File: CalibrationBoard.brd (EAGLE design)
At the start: 100 x 80 mm, 56 parts, among them Q1 N-HEXFET-2D_SOT232-, U1 MAX6225ACSA+, U2 MAX6250ACSA+, U3 MAX6126AASA50+

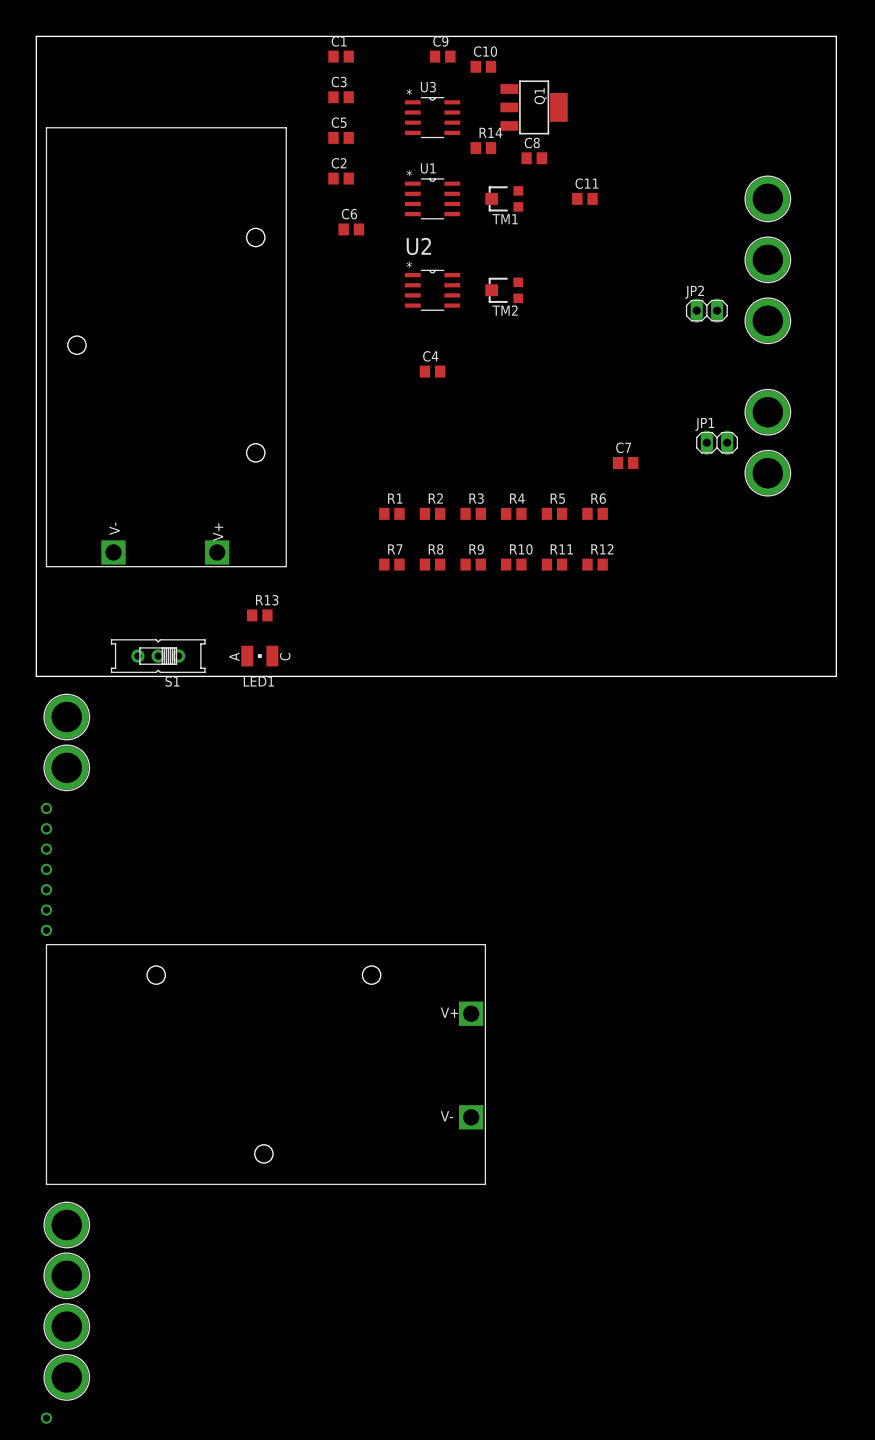
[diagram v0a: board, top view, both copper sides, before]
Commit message: Updates to CAD layout
moved TH to top side, SMDs are on bottom side
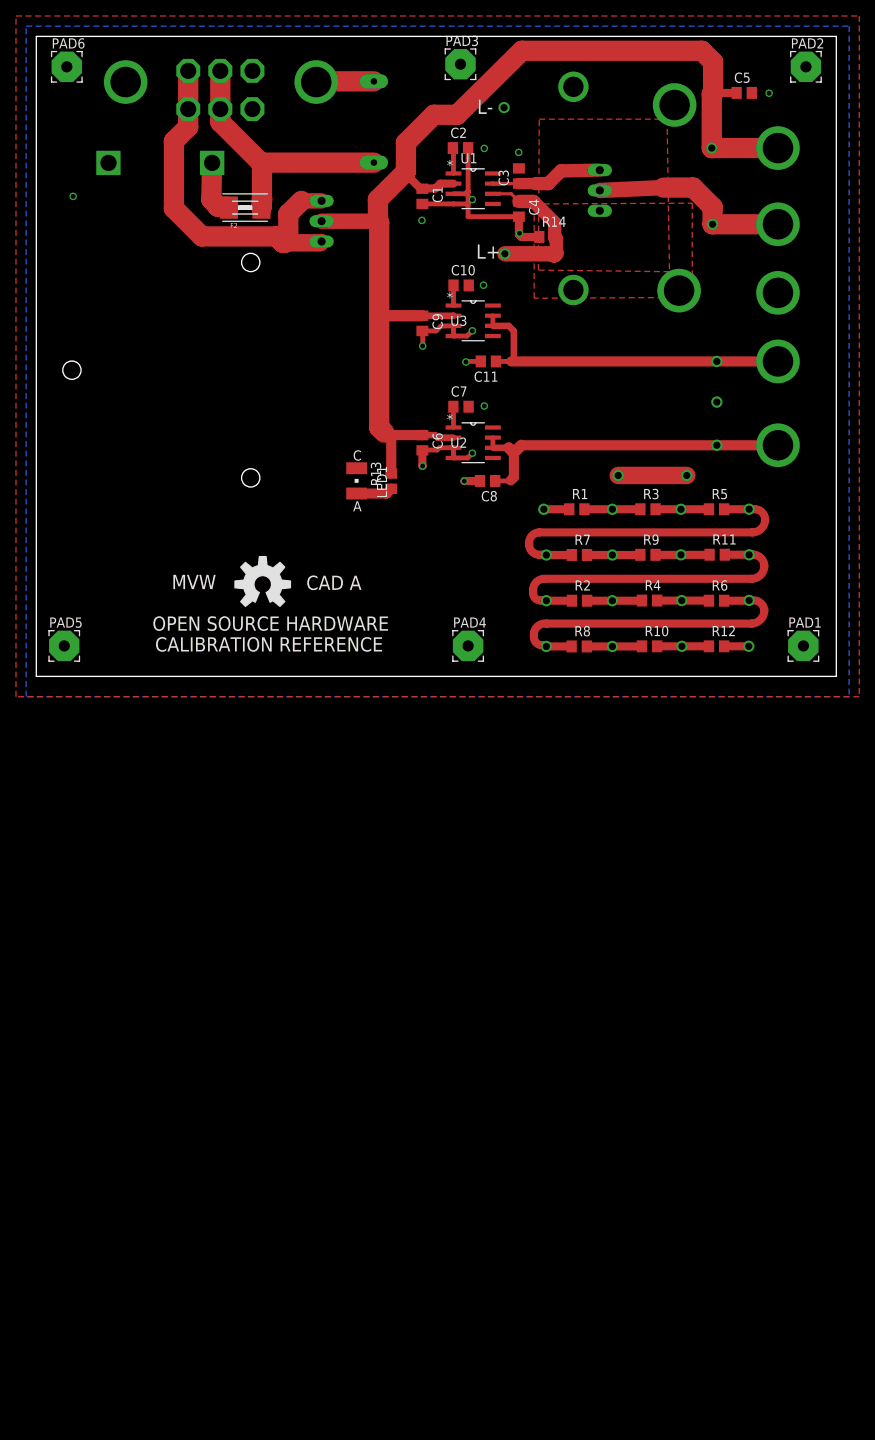
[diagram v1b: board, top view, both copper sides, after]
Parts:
- removed BAT2: (no value), SparkFun-Connectors:BC9VPC
- removed J10, J11: (no value), SparkFun-Connectors:BANANA_CONN
- removed JP1, JP2: (no value), pinhead:1X02
- removed S1: (no value), adafruit:EG1218
- removed TM1, TM2: 10k, adafruit:TC33X
- added D1: (no value), diode:TO220ABS
- added F1: 12A, fuse:LITTLEFUSE
- added F2: 1.1A, adafruit:1812
- added KK2: SK104-PAD, heatsink:SK104-PAD
- added LOGO1: OSHW-LOGOL, SparkFun-Aesthetics:OSHW-LOGO-L
- added PAD1, PAD2, PAD3, PAD4, PAD5, PAD6: (no value), wirepad:3,81/1,4
- added S3: 6A TOGGLE, switch:320-938
- added TP10, TP11, TP12, TP13, TP14, TP15, TP16, TP17, TP18, TP19, TP20, TP21, TP22, TP23, TP24, TP25, TP9: TP_1MM_TH", TP_1MM_TH:TP_1MM_TH
- BAT1: value (none) -> +9V_BATTERY
- C2, C7: value 2.2uF -> 1uF
- C5, C6: value 1uF -> 2.2uF
- J1, J2: value (none) -> BANANA SOCKET
- Q1: value N-HEXFET-2D_SOT232- -> IRF540; device transistor-power:SOT223 -> transistor-power:TO220BV
- R10: value 100k -> 1Meg
- R11: value 1Meg -> 100R
- R2: value 1R -> 1k
- R3: value 5R -> 1R
- R4: value 10R -> 5k
- R5: value 50R -> 5R
- R6: value 100R -> 10k
- R7: value 1k -> 10R
- R8: value 5k -> 100k
- R9: value 10k -> 50R
- U1: value MAX6225ACSA+ -> MAX6126AASA25+; device MAX6225ACSA+:SOIC127P600X175-8N -> MAX6126AASA50+:SOIC127P600X175-8N
- U2: value MAX6250ACSA+ -> MAX6126AASA25+; device MAX62250ACSA+:SOIC127P600X175-8N -> MAX6126AASA50+:SOIC127P600X175-8N
- moved J4 153.5 mm to (92.7, 56.5), flipped to the bottom
- moved J8 151.7 mm to (92.7, 47.9), flipped to the bottom
- moved TP8 133.8 mm to (72.0, 20.9), flipped to the bottom
- moved TP1 120.8 mm to (84.4, 66.0), flipped to the bottom
- moved J3 117.9 mm to (92.7, 66.0), flipped to the bottom
- moved TP2 115.9 mm to (84.5, 56.5), flipped to the bottom
- moved TP7 106.8 mm to (58.5, 71.1), flipped to the bottom
- moved TP4 96.7 mm to (81.3, 25.1), flipped to the bottom
- moved TP6 89.9 mm to (58.6, 52.8), flipped to the bottom
- moved TP3 88.3 mm to (72.7, 25.1), flipped to the bottom
- moved TP5 81.5 mm to (63.4, 20.9), flipped to the bottom
- moved J2 79.7 mm to (11.2, 74.3), flipped to the bottom
- moved J1 74.7 mm to (35.0, 74.3), flipped to the bottom
- moved BAT1 57.5 mm to (0.64, 11.1), flipped to the bottom, turned to 90 degrees
- moved C5 50.7 mm to (88.5, 72.9)
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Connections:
- removed net +2.5V_OUT: C7.1, J9.P$1, JP1.1, TP5.P$1, U1.6
- removed net +5.0V_OUT: C8.1, J7.P$1, JP2.1, TP3.P$1, U2.6
- removed net 18V_PWR: BAT2.V+, J4.P$1, S1.P
- removed net 9V_PWR: BAT1.V+, BAT2.V-, J8.P$1
- removed net N$1: TM2.2, U2.5
- removed net N$11: R2.2
- removed net N$25: J6.P$1, Q1.2, Q1.4, TP2.P$1
- removed net N$26: C9.1, Q1.1, U3.7
- removed net N$27: C10.1, J2.P$1, Q1.3, R14.2, TP6.P$1, U3.6
- removed net N$3: TM1.2, U1.5
- removed net N$7: C4.1, U2.3
- removed net V_IN: C11.1, C3.1, J5.P$1, TP1.P$1, U3.2
- new net +2.5V_REF: C8.1, J7.P$1, TP9.P$1, U2.6, U2.7
- new net +5.0V_REF: C11.1, J9.P$1, TP11.P$1, U3.6, U3.7
- new net +6V_IN: F1.1, J1.P$1
- new net N$15: C7.1, U2.1
- new net N$22: TP3.P$1, TP4.P$1
- new net N$6: C10.1, U3.1
- new net OUTF: C3.1, Q1.G, U1.7
- new net OUTS: C4.1, J5.P$1, Q1.S, R14.2, TP6.P$1, U1.6
- new net Q1_DRAIN: J4.P$1, Q1.D, TP2.P$1
- new net VIN_1: F1.2, F2.2, S3.2, S3.5
- new net V_IN2: C1.1, C5.1, C6.1, C9.1, D1.C, J3.P$1, R13.2, TP1.P$1, U1.2, U2.2, U3.2
- net GND: now also J2.P$1, J6.P$1, J8.P$1, KK2.K1, KK2.K2, PAD1.1, PAD2.1, PAD3.1, PAD4.1, PAD5.1, PAD6.1, TP10.P$1, U1.3, U2.3; no longer J1.P$1, J10.P$1, J11.P$1, J3.P$1, JP1.2, JP2.2, TM1.1, TM2.1, TP4.P$1, TP8.P$1
- net N$10: now also R3.1, TP8.P$1; no longer R2.1
- net N$12: now also R11.2, R2.1, TP15.P$1, TP24.P$1; no longer R6.2, R7.1
- net N$13: now also R2.2, R4.1, TP16.P$1; no longer R7.2, R8.1
- net N$16: now also R4.2, R6.1, TP17.P$1; no longer R8.2, R9.1
- net N$17: now also R10.1, R8.2, TP19.P$1; no longer R10.2, R11.1
- net N$18: now also R5.2, R7.1, TP12.P$1, TP13.P$1; no longer R3.2, R4.1
- net N$2: now also D1.A1, D1.A2, S3.3, S3.6; no longer C6.1, U1.3
- net N$21: now also R10.2, TP20.P$1; no longer R11.2
- net N$24: now also TP21.P$1
- net N$28: now also C2.1, U1.1; no longer C5.1, U3.1
- net N$29: now also R7.2, R9.1, TP14.P$1; no longer R4.2, R5.1
- net N$31: now also R3.2, R5.1, TP23.P$1; no longer R3.1
- net N$34: now also R6.2, R8.1, TP18.P$1, TP25.P$1; no longer R10.1, R9.2
- net N$5: now also TP5.P$1
- net N$8: now also R11.1, R9.2, TP22.P$1; no longer R5.2, R6.1
- net N$9: now also BAT1.V+, F2.1; no longer C1.1, C2.1, R13.2, S1.S, TM1.3, TM2.3, U1.2, U2.2
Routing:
- net V_IN2: track 0.00 -> 141.3 mm
- net GND: track 0.00 -> 51.2 mm, vias 0 -> 15
- net N$2: track 0.00 -> 46.8 mm
- net +5.0V_REF: track 0.00 -> 43.3 mm
- net +2.5V_REF: track 0.00 -> 43.1 mm
- net N$12: track 0.00 -> 42.5 mm
- net N$18: track 0.00 -> 42.4 mm
- net N$34: track 0.00 -> 41.1 mm
- net VIN_1: track 0.00 -> 34.4 mm
- net Q1_DRAIN: track 0.00 -> 25.4 mm
- net OUTS: track 0.00 -> 19.7 mm
- net OUTF: track 0.00 -> 14.0 mm
- net N$22: track 0.00 -> 8.57 mm
- net +6V_IN: track 0.00 -> 7.24 mm
- net N$9: track 0.00 -> 7.18 mm
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- added copper zone on layer 1, net GND
- added copper zone on layer 16, net GND
- added copper zone on layer 1, net OUTS
- added copper zone on layer 1, net Q1_DRAIN
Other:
- board text added: "(+6V)"
- board text added: "(0V)"
- board text added: "+2.5V"
- board text added: "+5.0V"
- board text added: "AMP+"
- board text added: "AMP-"
- board text added: "CAD A"
- board text added: "CALIBRATION REFERENCE"
- board text added: "GND"
- board text added: "L+"
- board text added: "L-"
- board text added: "LOAD+"
- board text added: "LOAD-"
- board text added: "MVW"
- board text added: "OPEN SOURCE HARDWARE"

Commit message: Added capacitors and inductors
Added capacitors and inductors and corrected some ERC errors
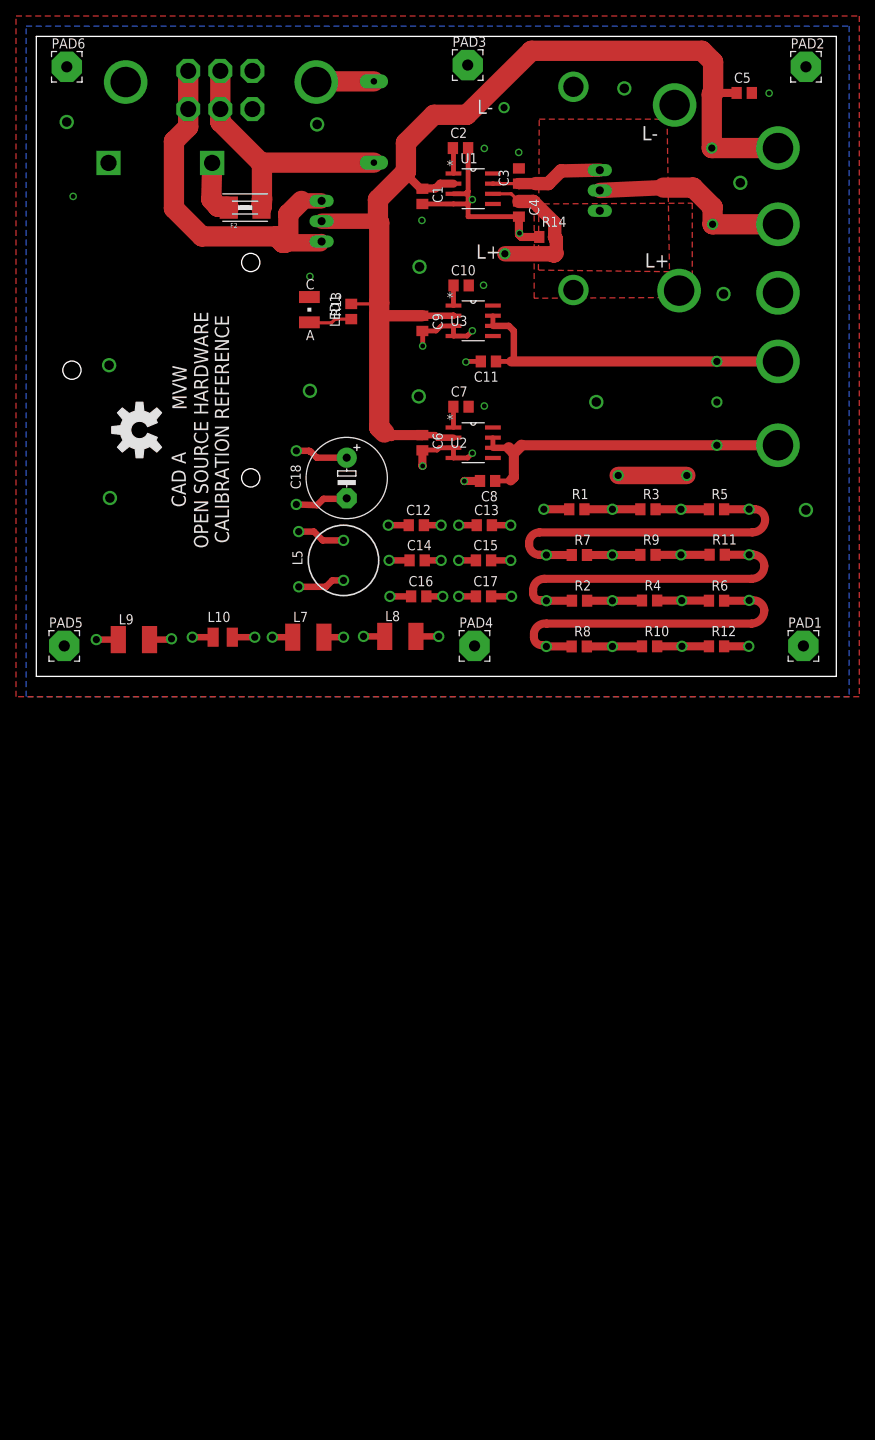
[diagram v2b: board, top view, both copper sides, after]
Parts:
- added C12: 10pF, rcl:C0805
- added C13: 1nF, rcl:C0805
- added C14: 10nF, rcl:C0805
- added C15: 100nF, rcl:C0805
- added C16: 1uF, rcl:C0805
- added C17: 100uF, rcl:C0805
- added C18: (no value), rcl:E5-10,5
- added L10: 330nH, rcl:L2825P
- added L5: 10mH, rcl:6000-XXXX-RC
- added L7: 1uH, rcl:L1812
- added L8: 100uH, rcl:L1812
- added L9: 1nH, rcl:L1812
- added TP26, TP27, TP28, TP29, TP30, TP31, TP32, TP33, TP34, TP35, TP36, TP37, TP38, TP39, TP41, TP42, TP43, TP44, TP45, TP46, TP47, TP48, TP49, TP51: TP_1MM_TH", TP_1MM_TH:TP_1MM_TH
- D1: value (none) -> 30A_MIN
- J1, J2: value BANANA SOCKET -> BANANA_CONN
- J3, J4, J5, J6, J7, J8, J9: value (none) -> BANANA_CONN
- LED1: value (none) -> GREEN_LED
- PAD1, PAD2, PAD3, PAD4, PAD5, PAD6: value (none) -> MOUNT_HOLE
- moved LOGO1 24.7 mm to (12.9, 30.8), turned to 90 degrees
- moved LED1 22.2 mm to (34.1, 45.8)
- moved R13 21.8 mm to (39.4, 45.6)
- moved PAD3 0.91 mm to (53.9, 76.4)
- moved PAD4 0.80 mm to (54.8, 3.81)
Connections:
- new net N$1: C12.1, TP26.P$1
- new net N$11: C17.2, TP30.P$1
- new net N$14: L7.2, TP37.P$1
- new net N$19: L8.2, TP38.P$1
- new net N$20: L5.2, TP39.P$1
- new net N$23: L9.1, TP42.P$1
- new net N$25: C18.+, TP41.P$1
- new net N$26: C18.-, TP51.P$1
- new net N$3: L9.2, TP35.P$1
- new net N$48: C12.2, TP27.P$1
- new net N$49: C13.2, TP32.P$1
- new net N$50: C14.2, TP33.P$1
- new net N$51: C15.2, TP29.P$1
- new net N$52: C16.2, TP31.P$1
- new net N$53: C13.1, TP34.P$1
- new net N$54: C14.1, TP44.P$1
- new net N$55: C15.1, TP46.P$1
- new net N$56: C16.1, TP47.P$1
- new net N$57: C17.1, TP48.P$1
- new net N$59: L5.1, TP43.P$1
- new net N$60: L8.1, TP49.P$1
- new net N$61: L7.1, TP45.P$1
- new net N$62: L10.1, TP28.P$1
- new net N$7: L10.2, TP36.P$1
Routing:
- net N$26: track 0.00 -> 6.66 mm
- net N$25: track 0.00 -> 6.66 mm
- net N$20: track 0.00 -> 6.06 mm
- net N$59: track 0.00 -> 5.93 mm
- net N$19: track 0.00 -> 2.85 mm
- net N$7: track 0.00 -> 2.80 mm
- net N$3: track 0.00 -> 2.79 mm
- net N$23: track 0.00 -> 2.75 mm
- net N$60: track 0.00 -> 2.65 mm
- net N$56: track 0.00 -> 2.65 mm
- net N$62: track 0.00 -> 2.60 mm
- net N$61: track 0.00 -> 2.55 mm
- net N$54: track 0.00 -> 2.55 mm
- net N$11: track 0.00 -> 2.55 mm
- net N$1: track 0.00 -> 2.55 mm
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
